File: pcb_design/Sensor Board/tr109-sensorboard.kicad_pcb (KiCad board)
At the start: 2 copper layers, 65 x 30 mm, 56 parts, among them J1 Conn_01x01_Female, J2 Conn_01x01_Female, J3 Conn_01x04_Female, J47 Raspberry_Pi_2_3, U1 BME680, U2 74HC595, U3 AMG8833

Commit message: Pcb and shell design work
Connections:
- J47 pad 31: Shift_Latch -> Net-(J47-Pad31)
- J47 pad 35: Net-(J47-Pad35) -> Shift_Serial
- J47 pad 36: Shift_Serial -> Net-(J47-Pad36)
- J47 pad 37: Net-(J47-Pad37) -> Shift_Clock
- J47 pad 38: Shift_Clock -> Net-(J47-Pad38)
- J47 pad 40: Net-(J47-Pad40) -> Shift_Latch
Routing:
- net Shift_Latch: track 21.5 -> 11.7 mm
- net Shift_Serial: track 17.6 -> 13.1 mm
- net Shift_Clock: track 12.5 -> 8.88 mm
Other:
- outline, holes or cut-outs redrawn

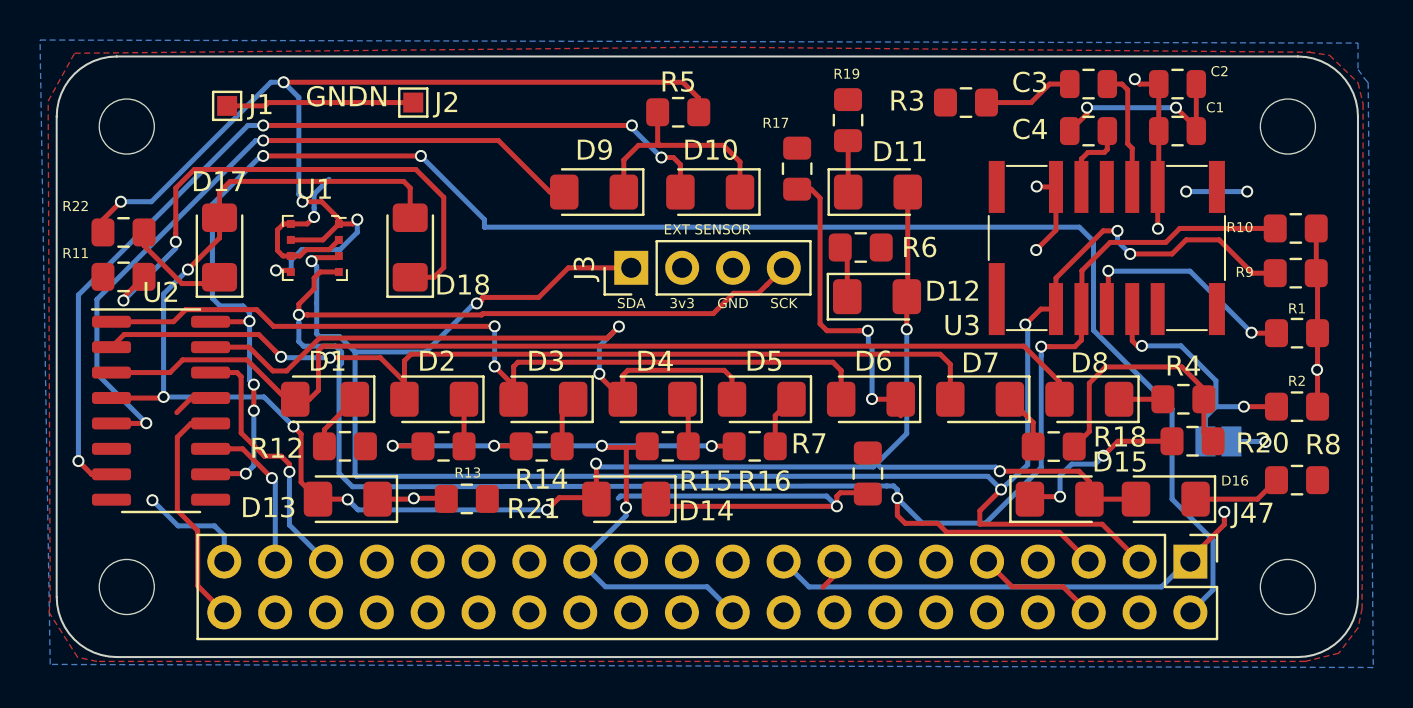
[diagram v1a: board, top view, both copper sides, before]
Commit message: Rev 3 board changes, blender file changes
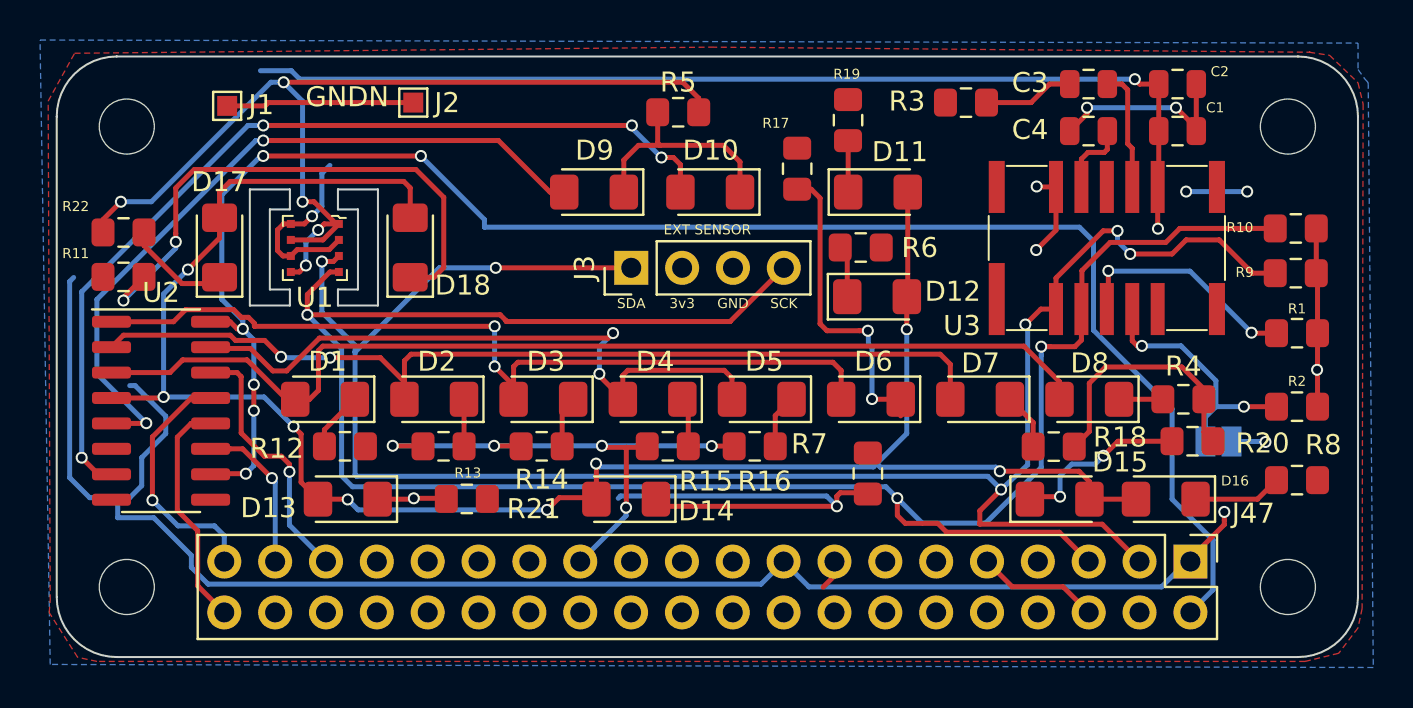
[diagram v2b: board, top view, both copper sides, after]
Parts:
- added G***: Picorder Logo, Logos:Untitled, B.Cu at (143.8, 109.6)
- D1, D10, D2, D3, D4, D5, D6, D7, D8, D9: value LED -> G-LED
- D11, D12: value LED -> R-LED
- D13, D14, D17, D18: value LED -> B-LED
- D15, D16: value LED -> Y-LED
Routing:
- net 3.3V: track 55.4 -> 157.1 mm
- net GND: track 132.0 -> 124.6 mm
- net SCK: track 109.6 -> 107.5 mm
- net SDA: track 99.7 -> 98.0 mm
- net 5V: track 87.4 -> 86.1 mm
- net ALPHA: track 34.3 -> 33.4 mm
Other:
- outline, holes or cut-outs redrawn
- board text added: "TBH/VOC/EXP/TC - REV 3"
- board text removed: "MK1 - TBH/VOC/IMU/TC - REV 2"
